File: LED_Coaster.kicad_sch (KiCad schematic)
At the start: 48 parts, among them IC1 ESP32-WROOM-32E-N4, IC2 VCNL4010-GS08, J1 JST_2P_1769, J3 micro_usb_female_105164-0001, Q1 DMG3415U, Q2 MBT2222ADW1T1, U1 AP2112-3.3, U2 CP2104, U3 MCP73831-2-OT

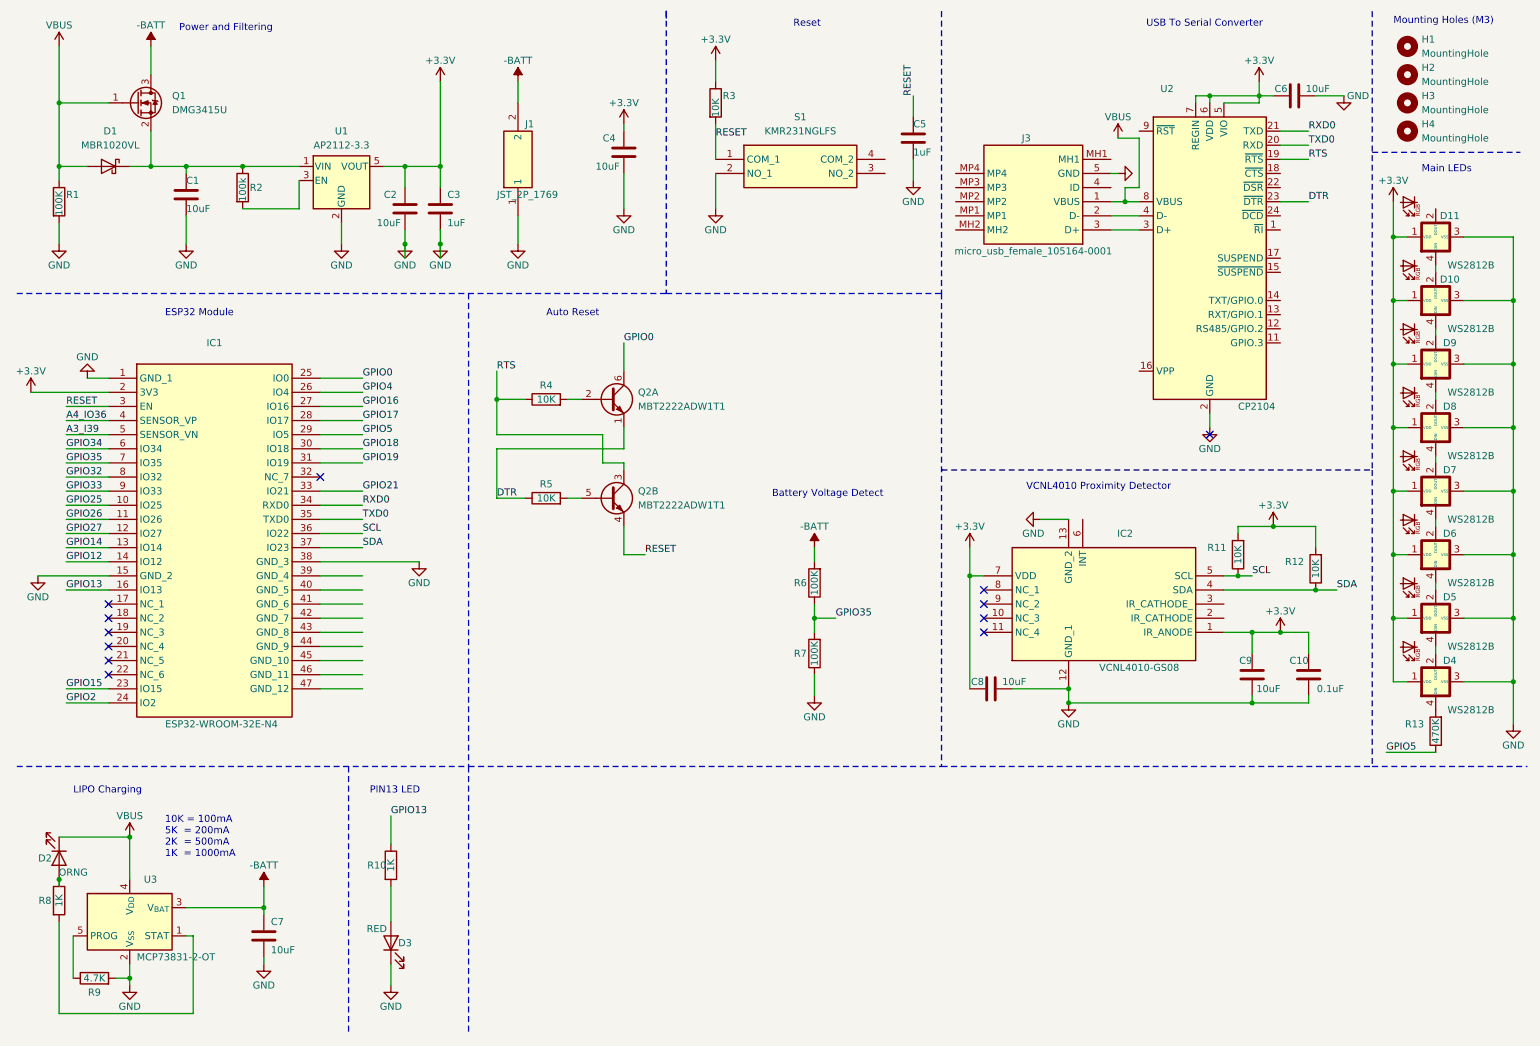
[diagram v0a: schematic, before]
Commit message: Rerouted some traces, changed diode to a standard 0.7/0.8V drop, tried to improve power routing. Fixed "-VBATT" to "+VBATT"
My work is a bit messy still, but it should be fine like this. Still haven't done the math on the LDO, need to figure out what the power of the system is.
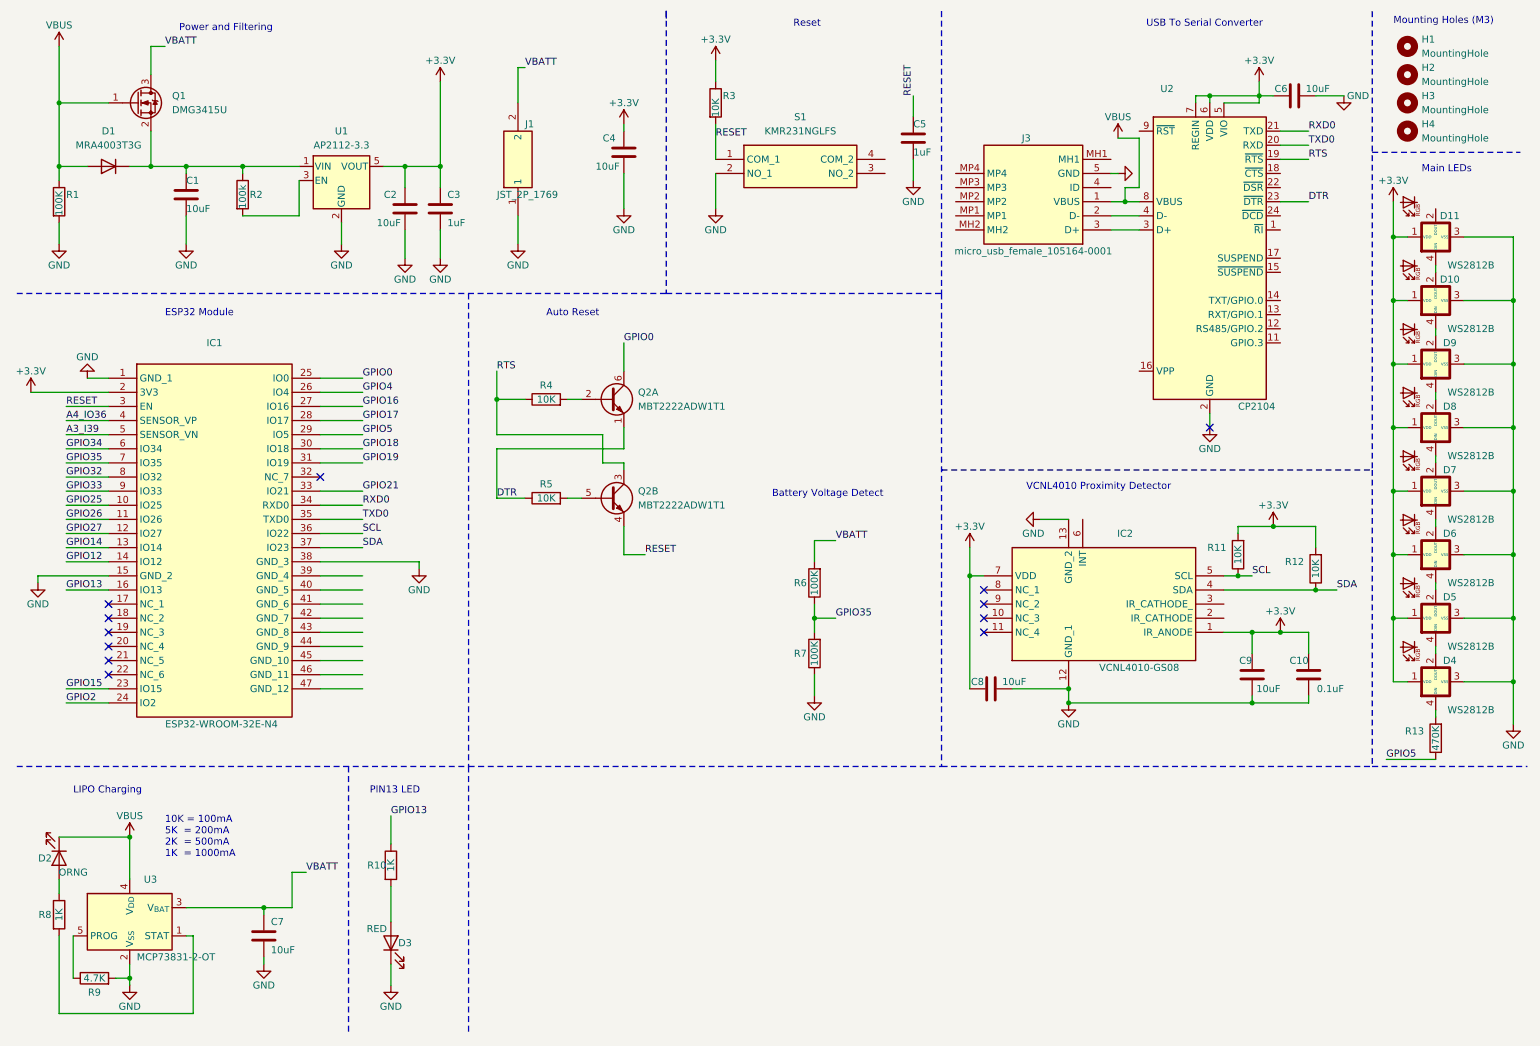
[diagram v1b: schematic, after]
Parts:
- removed D1: MBR1020VL, Diode_SMD:D_SOD-123F, symbol Diode:MBR1020VL
- added D1: MRA4003T3G, Diode_SMD:D_SMA, symbol Diode:MRA4003T3G
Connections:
- net VBUS: now also D1.2 (A)
- net at C1.1, Q1.2 (S), R2.1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: now also D1.1 (K)
- net -BATT renamed VBATT
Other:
- moved on the sheet: R13, R2, R8
